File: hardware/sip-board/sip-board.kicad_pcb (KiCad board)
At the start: 8 copper layers, 92 parts, among them IC1 XC7S15-1CPGA196C, IC2 MT25QL512ABB1EW9-0SIT, J1 Conn_02x03_Odd_Even, J2 Conn_01x10_Pin, J3 Conn_01x10_Pin, J4 Conn_01x10_Pin, J5 Conn_01x10_Pin, U1 TLV75718PDRV, U2 TLV75733PDRV, U3 TLV75710PDRV

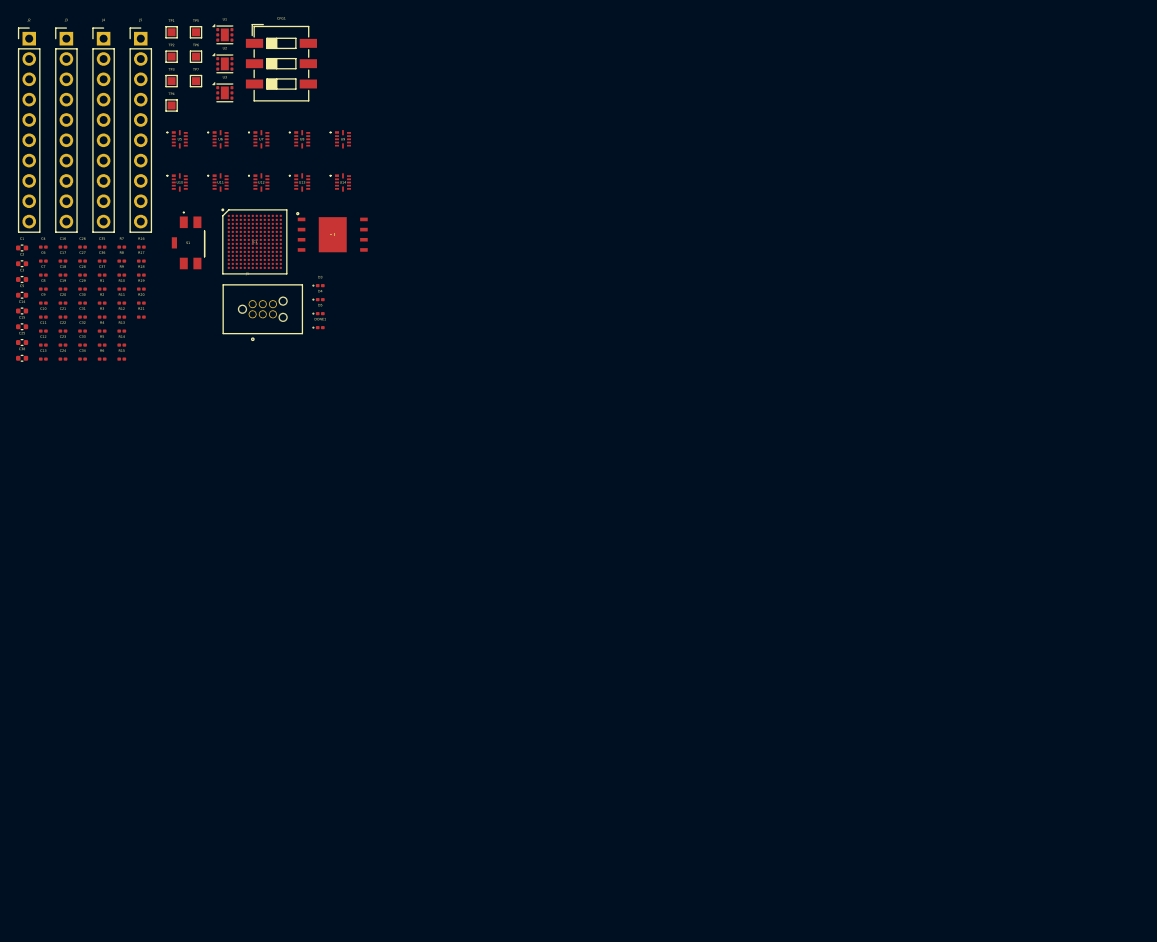
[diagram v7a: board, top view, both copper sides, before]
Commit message: placement done, new dip switch
need to start picking parts and routing
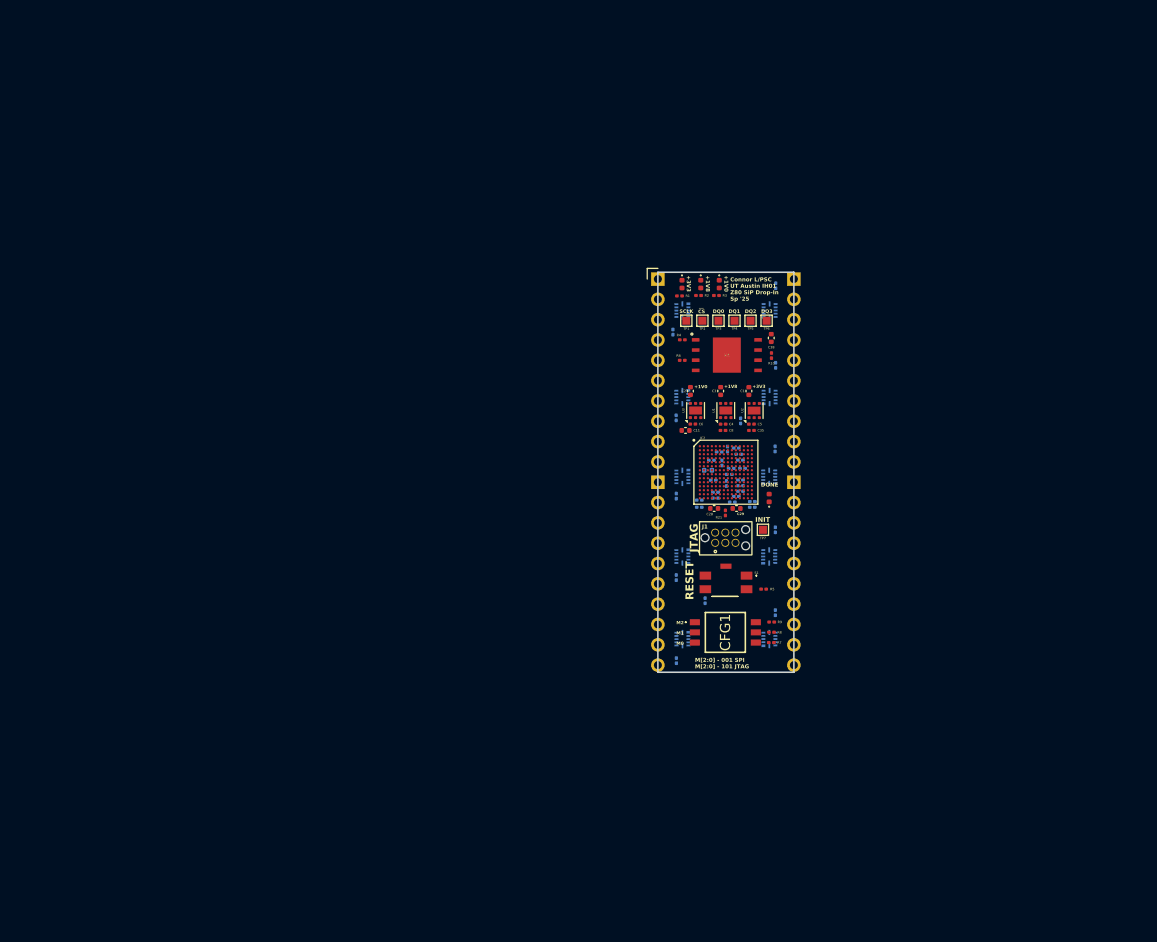
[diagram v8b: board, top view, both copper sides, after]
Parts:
- removed D4, D5: LED, LED_SMD:LED_0201_0603Metric
- removed U14: ~, hardware:NXB0104GU12X
- added D1: LED, LED_SMD:LED_0402_1005Metric, F.Cu at (103.0, 51.5)
- added D2: LED, LED_SMD:LED_0402_1005Metric, F.Cu at (105.4, 51.5)
- added U4: ~, hardware:NXB0104GU12X, B.Cu at (103.1, 75.6)
- C10, C13, C31, C32, C33, C34: value 0.47u -> 4.7u; moved to B.Cu
- C11: value 10u -> 100u; footprint Capacitor_SMD:C_0201_0603Metric -> Capacitor_SMD:C_0402_1005Metric
- C12, C20, C21, C22, C23, C36, C7, C9, R11, R12, R13, U10, U11, U12, U13, U5, U6, U7, U8, U9: moved to B.Cu
- C14, C25: value 100u -> 0.47u; footprint Capacitor_SMD:C_0402_1005Metric -> Capacitor_SMD:C_0201_0603Metric; moved to B.Cu
- C15: value 100u -> 4.7u; footprint Capacitor_SMD:C_0402_1005Metric -> Capacitor_SMD:C_0201_0603Metric; moved to B.Cu
- C16, C17, C18, C19, C26, C27: value 4.7u -> 0.47u; moved to B.Cu
- C2, C3: value 50u -> 10u
- C24: value 47u -> 0.47u; moved to B.Cu
- C28: value 0.47u -> 100u; footprint Capacitor_SMD:C_0201_0603Metric -> Capacitor_SMD:C_0402_1005Metric
- C29: value 4.7u -> 100u; footprint Capacitor_SMD:C_0201_0603Metric -> Capacitor_SMD:C_0402_1005Metric
- C30: value 0.47u -> 100u; footprint Capacitor_SMD:C_0201_0603Metric -> Capacitor_SMD:C_0402_1005Metric; moved to B.Cu
- C35: value 100u -> 4.7u
- C37: value 4.7u -> 10u; moved to B.Cu
- C4, C6: value 1u -> 100u
- C5: footprint Capacitor_SMD:C_0402_1005Metric -> Capacitor_SMD:C_0201_0603Metric
- C8: value 0.47u -> 47u
- CFG1: footprint Button_Switch_SMD:SW_DIP_SPSTx03_Slide_6.7x9.18mm_W6.73mm_P2.54mm_LowProfile_JPin -> hardware:WE-3-SPST-DIP
- D3, DONE1: footprint LED_SMD:LED_0201_0603Metric -> LED_SMD:LED_0402_1005Metric
- IC1: value XC7S15-1CPGA196C -> MT25QL512ABB1EW9-0SIT; footprint fpga_stuff:BGA196C50P14X14_800X800X110 -> hardware:MT25QL512ABB1EW9-0SIT
- IC2: value MT25QL512ABB1EW9-0SIT -> XC7S15-1CPGA196C; footprint hardware:MT25QL512ABB1EW9-0SIT -> fpga_stuff:BGA196C50P14X14_800X800X110
- R1, R2, R3: value 1k -> R_Small
- R10, R4, R5, R6: value 10k -> 4k7
- R14, R15, R16, R17: value 4k7 -> 10k; moved to B.Cu
- R18: value 2k3 -> 10k; moved to B.Cu
- R19: value 3k -> 10k; moved to B.Cu
- R20: value 5k7 -> 10k; moved to B.Cu
- R7, R8, R9: value 10k -> 1k
- moved J4 102.6 mm to (117.0, 76.2)
- moved R7 95.1 mm to (114.2, 96.3)
- moved C38 93.7 mm to (114.2, 58.2), turned to -90 degrees
- moved R8 93.5 mm to (114.2, 95.0)
- moved C1 92.6 mm to (111.4, 64.8), turned to 90 degrees
- moved C5 92.6 mm to (111.7, 69.0)
- moved J3 92.4 mm to (100.0, 76.2)
- moved R9 92.1 mm to (114.2, 93.7)
- moved TP7 90.4 mm to (113.1, 82.2)
- moved CFG1 90.2 mm to (108.4, 95.0), turned to -90 degrees
- moved C17 89.2 mm to (110.3, 76.7)
- moved C9 88.9 mm to (110.1, 72.7)
- moved C14 88.9 mm to (107.7, 72.5), turned to 180 degrees
- moved C25 88.7 mm to (107.2, 77.5), turned to 180 degrees
- moved C15 88.5 mm to (106.9, 76.0), turned to 180 degrees
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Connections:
- C10 pad 1: +3V3 -> +1V8
- C11 pad 1: Net-(S1-COM_2) -> +1V0
- C12 pad 1: +1V0 -> +1V8
- C13 pad 1: +3V3 -> +1V0
- C14 pad 1: +1V0 -> +1V8
- C15 pad 1: +3V3 -> +1V0
- C16 pad 1: +1V0 -> +3V3
- C18 pad 1: +1V0 -> +3V3
- C24 pad 1: +1V8 -> +3V3
- C26 pad 1: +1V8 -> +3V3
- C28 pad 1: +1V8 -> +3V3
- C30 pad 1: +1V8 -> +3V3
- C37 pad 1: +3V3 -> Net-(S1-COM_2)
- C7 pad 1: +3V3 -> +1V0
- C8 pad 1: +3V3 -> +1V8
- R1 pad 1: M0_CONFIG -> +3V3
- R1 pad 2: GND -> Net-(D1-A)
- R10 pad 2: Net-(U11-OE) -> SPI_DQ3
- R11 pad 2: Net-(U12-OE) -> Net-(U4-OE)
- R12 pad 2: Net-(U13-OE) -> Net-(U5-OE)
- R13 pad 2: Net-(U14-OE) -> Net-(U6-OE)
- R14 pad 2: PROGRAM_B -> Net-(U7-OE)
- R15 pad 2: SPI_CS -> Net-(U8-OE)
- R16 pad 2: INIT_B -> Net-(U9-OE)
- R17 pad 2: SPI_DQ3 -> Net-(U10-OE)
- R18 pad 1: Net-(D3-A) -> +3V3
- R18 pad 2: +1V0 -> Net-(U11-OE)
- R19 pad 1: Net-(D4-A) -> +3V3
- R19 pad 2: +1V8 -> Net-(U12-OE)
- R2 pad 1: M1_CONFIG -> +1V8
- R2 pad 2: GND -> Net-(D2-A)
- R20 pad 1: Net-(D5-A) -> +3V3
- R20 pad 2: +3V3 -> Net-(U13-OE)
- R21 pad 2: SPI_DQ2 -> INIT_B
- R3 pad 1: M2_CONFIG -> +1V0
- R3 pad 2: GND -> Net-(D3-A)
- R4 pad 2: Net-(U5-OE) -> SPI_CS
- R5 pad 2: Net-(U6-OE) -> PROGRAM_B
- R6 pad 2: Net-(U7-OE) -> SPI_DQ2
- R7 pad 1: +3V3 -> M0_CONFIG
- R7 pad 2: Net-(U8-OE) -> GND
- R8 pad 1: +3V3 -> M1_CONFIG
- R8 pad 2: Net-(U9-OE) -> GND
- R9 pad 1: +3V3 -> M2_CONFIG
- R9 pad 2: Net-(U10-OE) -> GND
- S1 pad 5: Net-(S1-COM_2) -> GND
- TP1 pad 1: INIT_B -> SPI_SCK_CCLK
- TP2 pad 1: SPI_SCK_CCLK -> SPI_CS
- TP3 pad 1: SPI_CS -> SPI_DQ0
- TP4 pad 1: SPI_DQ0 -> SPI_DQ1
- TP5 pad 1: SPI_DQ1 -> SPI_DQ2
- TP6 pad 1: SPI_DQ2 -> SPI_DQ3
- TP7 pad 1: SPI_DQ3 -> INIT_B
- U10 pad 10: BUSAK_5V -> A4_5V
- U10 pad 11: WAIT_5V -> A3_5V
- U10 pad 2: WAIT_FPGA -> A3_FPGA
- U10 pad 3: BUSAK_FPGA -> A4_FPGA
- U10 pad 4: WR_FPGA -> A5_FPGA
- U10 pad 5: RD_FPGA -> A6_FPGA
- U10 pad 8: RD_5V -> A6_5V
- U10 pad 9: WR_5V -> A5_5V
- U11 pad 10: M1_5V -> A1_5V
- U11 pad 11: RFSH_5V -> A0_5V
- U11 pad 2: RFSH_FPGA -> A0_FPGA
- U11 pad 3: M1_FPGA -> A1_FPGA
- U11 pad 4: RESET_FPGA -> A2_FPGA
- U11 pad 5: BUSRQ_FPGA -> unconnected-(U11-A4-Pad5)
- U11 pad 8: BUSRQ_5V -> unconnected-(U11-B4-Pad8)
- U11 pad 9: RESET_5V -> A2_5V
- U12 pad 10: A1_5V -> RESET_5V
- U12 pad 11: A2_5V -> BUSRQ_5V
- U12 pad 2: A2_FPGA -> BUSRQ_FPGA
- U12 pad 3: A1_FPGA -> RESET_FPGA
- U12 pad 4: A0_FPGA -> M1_FPGA
- U12 pad 5: unconnected-(U12-A4-Pad5) -> RFSH_FPGA
- U12 pad 8: unconnected-(U12-B4-Pad8) -> RFSH_5V
- U12 pad 9: A0_5V -> M1_5V
- U13 pad 10: A5_5V -> WR_5V
- U13 pad 11: A6_5V -> RD_5V
- U13 pad 2: A6_FPGA -> RD_FPGA
- U13 pad 3: A5_FPGA -> WR_FPGA
- U13 pad 4: A4_FPGA -> BUSAK_FPGA
- U13 pad 5: A3_FPGA -> WAIT_FPGA
- U13 pad 8: A3_5V -> WAIT_5V
- U13 pad 9: A4_5V -> BUSAK_5V
- U2 pad 4: +5V -> +1V8
- U5 pad 10: A12_5V -> D0_5V
- U5 pad 11: A11_5V -> D7_5V
- U5 pad 2: A11_FPGA -> D7_FPGA
- U5 pad 3: A12_FPGA -> D0_FPGA
- U5 pad 4: A13_FPGA -> D1_FPGA
- U5 pad 5: A14_FPGA -> INT_FPGA
- U5 pad 8: A14_5V -> INT_5V
- U5 pad 9: A13_5V -> D1_5V
- U7 pad 10: D6_5V -> HALT_5V
- U7 pad 11: D5_5V -> NMI_5V
- U7 pad 2: D5_FPGA -> NMI_FPGA
- U7 pad 3: D6_FPGA -> HALT_FPGA
- U7 pad 4: unconnected-(U7-A3-Pad4) -> MREQ_FPGA
- U7 pad 5: D2_FPGA -> IORQ_FPGA
- U7 pad 8: D2_5V -> IORQ_5V
- U7 pad 9: unconnected-(U7-B3-Pad9) -> MREQ_5V
- U8 pad 10: D0_5V -> A12_5V
- U8 pad 11: D7_5V -> A11_5V
- U8 pad 2: D7_FPGA -> A11_FPGA
- U8 pad 3: D0_FPGA -> A12_FPGA
- U8 pad 4: D1_FPGA -> A13_FPGA
- U8 pad 5: INT_FPGA -> A14_FPGA
- U8 pad 8: INT_5V -> A14_5V
- U8 pad 9: D1_5V -> A13_5V
- U9 pad 10: HALT_5V -> A8_5V
- U9 pad 11: NMI_5V -> A7_5V
- U9 pad 2: NMI_FPGA -> A7_FPGA
- U9 pad 3: HALT_FPGA -> A8_FPGA
- U9 pad 4: MREQ_FPGA -> A9_FPGA
- U9 pad 5: IORQ_FPGA -> A10_FPGA
- U9 pad 8: IORQ_5V -> A10_5V
- U9 pad 9: MREQ_5V -> A9_5V
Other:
- board outline added: 17 x 50 mm
- board text added: "+1V0"
- board text added: "+1V8"
- board text added: "+3V3"
- board text added: "Board is 17mm wide x 50mm tall and top left is at (100, 50) Connectors holes 1.7mm diameter/width, 2.54mm pitch. Then, placement is: (100, 50 + 1.7/2) - Pins 1-10 (100, 50 + (10*2.54) + (1.7/2)) - Pins 11-20 (117, 50 + 1.7/2) - Pins 21-30 (117, 50 + (10*2.54) + (1.7/2)) - Pins 31-40"
- board text added: "CS"
- board text added: "Connor L/PSC UT Austin IH01 Z80 SiP Drop-In Sp '25"
- board text added: "DONE"
- board text added: "DQ0"
- board text added: "DQ1"
- board text added: "DQ2"
- board text added: "DQ3"
- board text added: "INIT"
- board text added: "JTAG"
- board text added: "M2 M1 M0"
- board text added: "M[2:0] - 001 SPI M[2:0] - 101 JTAG"
- board text added: "RESET"
- board text added: "SCLK"
- board text added: "__"
